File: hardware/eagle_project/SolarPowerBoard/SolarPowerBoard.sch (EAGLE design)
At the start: 77 parts, among them IC1 BQ29700DSET, IC3 TPS63031DSKT, J2 105017-0001, J5 XG8S-0331, K1 G6E-134P-US_DC5, Q3 FDN302P, U4 MCP73831T-2ACI/OT

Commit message: First check. Few things to modify:
- rearrange kelvin connections on sensing resistor (and routing around the fuel gauge)
- add LED on CBUS1 and CBUS2 of the FTDI chip (see powerDevPack project), or remove the CBUS1 and CBUS2 connections
- edit the JST connector footprint and increase holes size (see J5 footprint as reference)
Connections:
- net N$31 renamed USBDR_N
- net N$32 renamed USBDR_P
- net GND: no longer CHG2.EP, DCH2.EP
- net N$14: now also CHG2.EP, DCH2.EP
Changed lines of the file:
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@@
 <part name="GND32" library="supply1" library_urn="urn:adsk.eagle:library:371" deviceset="GND" device=""/>
 <part name="GND36" library="supply1" library_urn="urn:adsk.eagle:library:371" deviceset="GND" device=""/>
-<part name="GND23" library="supply1" library_urn="urn:adsk.eagle:library:371" deviceset="GND" device=""/>
-<part name="GND26" library="supply1" library_urn="urn:adsk.eagle:library:371" deviceset="GND" device=""/>
 <part name="J4" library="SolarComponents" deviceset="JST_2MM_MALE" device=""/>
 <part name="J3" library="SparkFun-Connectors" deviceset="CONN_01" device=""/>
@@
 <attribute name="VALUE" x="33.02" y="-30.48" size="1.778" layer="96" rot="R90"/>
 </instance>
-<instance part="GND23" gate="1" x="414.02" y="-20.32">
-<attribute name="VALUE" x="411.48" y="-22.86" size="1.778" layer="96"/>
-</instance>
-<instance part="GND26" gate="1" x="487.68" y="-20.32">
-<attribute name="VALUE" x="485.14" y="-22.86" size="1.778" layer="96"/>
-</instance>
 <instance part="J4" gate="G$1" x="479.806" y="46.99" rot="R90">
 <attribute name="NAME" x="473.964" y="44.45" size="1.778" layer="95" rot="R90"/>
@@
 <wire x1="17.78" y1="-27.94" x2="27.94" y2="-27.94" width="0.1524" layer="91"/>
 <pinref part="GND36" gate="1" pin="GND"/>
-</segment>
-<segment>
-<pinref part="CHG2" gate="G$1" pin="EP"/>
-<wire x1="414.02" y1="-12.7" x2="414.02" y2="-17.78" width="0.1524" layer="91"/>
-<pinref part="GND23" gate="1" pin="GND"/>
-</segment>
-<segment>
-<pinref part="DCH2" gate="G$1" pin="EP"/>
-<wire x1="487.68" y1="-12.7" x2="487.68" y2="-17.78" width="0.1524" layer="91"/>
-<pinref part="GND26" gate="1" pin="GND"/>
 </segment>
 <segment>
@@
 </segment>
 </net>
-<net name="N$31" class="0">
+<net name="USBDR_N" class="0">
 <segment>
 <pinref part="R23" gate="G$1" pin="1"/>
@@
 <wire x1="60.96" y1="152.4" x2="66.04" y2="152.4" width="0.1524" layer="91"/>
 <wire x1="66.04" y1="152.4" x2="66.04" y2="151.13" width="0.1524" layer="91"/>
-</segment>
-</net>
-<net name="N$32" class="0">
+<label x="60.96" y="152.4" size="1.778" layer="95"/>
+</segment>
+</net>
+<net name="USBDR_P" class="0">
 <segment>
 <pinref part="FT230XQ-R" gate="G$1" pin="USBDP"/>
@@
 <wire x1="66.04" y1="148.59" x2="66.04" y2="147.32" width="0.1524" layer="91"/>
 <wire x1="66.04" y1="147.32" x2="60.96" y2="147.32" width="0.1524" layer="91"/>
+<label x="58.42" y="144.78" size="1.778" layer="95"/>
 </segment>
 </net>
@@
 <wire x1="457.2" y1="10.16" x2="454.66" y2="10.16" width="0.1524" layer="91"/>
 <junction x="454.66" y="10.16"/>
-</segment>
-</net>
+<pinref part="CHG2" gate="G$1" pin="EP"/>
+<wire x1="414.02" y1="-12.7" x2="447.04" y2="-12.7" width="0.1524" layer="91"/>
+<wire x1="447.04" y1="-12.7" x2="447.04" y2="-5.08" width="0.1524" layer="91"/>
+<junction x="447.04" y="-5.08"/>
+<pinref part="DCH2" gate="G$1" pin="EP"/>
+<wire x1="487.68" y1="-12.7" x2="454.66" y2="-12.7" width="0.1524" layer="91"/>
+<wire x1="454.66" y1="-12.7" x2="454.66" y2="-5.08" width="0.1524" layer="91"/>
+<junction x="454.66" y="-5.08"/>
+</segment>
+</net>

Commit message: Fixed library link. Several small problems fixed.
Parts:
- added R27, R28: 470, SparkFun-Resistors:0.3OHM-0805-1/8W-1%
- added RX: ORANGE, SparkFun-LED:LED0603
- added TX: YELLOW, SparkFun-LED:LED0603
- AND: value 74AHC1G08DCK -> 74XX-LITTLE-DE_74AHC1G08DCK; device 74xx-little-de:74AHC1G08DCK -> SolarPowerBoard:74XX-LITTLE-DE_74AHC1G08DCK
- C1, C7, CMPP: device SparkFun-Capacitors:0.1UF-0603-100V-10% -> SolarPowerBoard:SPARKFUN-CAPACITORS_0.1UF-0603-100V-10%
- C1-1, C1-2: device SparkFun-Capacitors:4.7UF0603 -> SolarPowerBoard:SPARKFUN-CAPACITORS_4.7UF0603
- C10, COUT1, COUT2: device resistor:C-EUC0805 -> SolarPowerBoard:RESISTOR_C-EUC0805
- C11, C12: device SparkFun-Capacitors:CAP0603-CAP -> SolarPowerBoard:SPARKFUN-CAPACITORS_CAP0603-CAP
- C14: value 10uF -> 10nF; device SparkFun-Capacitors:10UF-0805-10V-10% -> SolarPowerBoard:SPARKFUN-CAPACITORS_10UF-0805-10V-10%:1
- C15, C16: value 10uF -> 47pF; device SparkFun-Capacitors:10UF-0805-10V-10% -> SolarPowerBoard:SPARKFUN-CAPACITORS_10UF-0805-10V-10%:1
- C2, C4: device SparkFun-Capacitors:10UF-0805-10V-10% -> SolarPowerBoard:SPARKFUN-CAPACITORS_10UF-0805-10V-10%
- C24, C26, C8, C9: value 10uF -> 100nF; device SparkFun-Capacitors:10UF-0805-10V-10% -> SolarPowerBoard:SPARKFUN-CAPACITORS_10UF-0805-10V-10%:1
- C25: value 10uF -> 4.7uF; device SparkFun-Capacitors:10UF-0805-10V-10% -> SolarPowerBoard:SPARKFUN-CAPACITORS_10UF-0805-10V-10%:1
- C3: value 10UF -> 10uF; device SparkFun-Capacitors:10UF-0805-10V-10% -> SolarPowerBoard:SPARKFUN-CAPACITORS_10UF-0805-10V-10%
- C5: device SparkFun-Capacitors:0.1UF-0603-25V-5% -> SolarPowerBoard:SPARKFUN-CAPACITORS_0.1UF-0603-25V-5%
- C6: device SparkFun-Capacitors:470PF-0603-50V-5% -> SolarPowerBoard:SPARKFUN-CAPACITORS_470PF-0603-50V-5%
- CF: device SparkFun-Capacitors:1.0UF-0805-25V-(+80/-20%) -> SolarPowerBoard:SPARKFUN-CAPACITORS_1.0UF-0805-25V-(+80/-20%)
- CHG2, DCH2: value CSD16406Q3 -> SOLARCOMPONENTS_CSD16406Q3; device SolarComponents:CSD16406Q3 -> SolarPowerBoard:SOLARCOMPONENTS_CSD16406Q3
- D5: device SparkFun-LED:LED0603 -> SolarPowerBoard:SPARKFUN-LED_LED0603
- FT230XQ-R: device FT230XQ:FT230XQ_2 -> SolarPowerBoard:FT230XQ_FT230XQ_2
- IC1: value BQ29700DSET -> BQ29700DSET_BQ29700DSET; device BQ29700DSET:BQ29700DSET -> SolarPowerBoard:BQ29700DSET_BQ29700DSET
- IC3: value TPS63031DSKT -> TPS63031DSKT_TPS63031DSKT; device TPS63031DSKT:TPS63031DSKT -> SolarPowerBoard:TPS63031DSKT_TPS63031DSKT
- J2: value 105017-0001 -> 105017-0001_105017-0001; device 105017-0001:105017-0001 -> SolarPowerBoard:105017-0001_105017-0001
- J3: device SparkFun-Connectors:CONN_01 -> SolarPowerBoard:SPARKFUN-CONNECTORS_CONN_01
- J4, J6: device SolarComponents:JST_2MM_MALE -> SolarPowerBoard:SOLARCOMPONENTS_JST_2MM_MALE
- J5: value XG8S-0331 -> XG8S-0331_XG8S-0331; device XG8S-0331:XG8S-0331 -> SolarPowerBoard:XG8S-0331_XG8S-0331
- JP1: value JUMPER-SMT_3_1-NC_TRACE_NO-SILK -> SPARKFUN-JUMPERS_JUMPER-SMT_3_1-NC_TRACE_NO-SILK; device SparkFun-Jumpers:JUMPER-SMT_3_1-NC_TRACE_NO-SILK -> SolarPowerBoard:SPARKFUN-JUMPERS_JUMPER-SMT_3_1-NC_TRACE_NO-SILK
- K1: value G6E-134P-US_DC5 -> G6E-134P-US_DC5_G6E-134P-US_DC5; device G6E-134P-US_DC5:G6E-134P-US_DC5 -> SolarPowerBoard:G6E-134P-US_DC5_G6E-134P-US_DC5
- L1: value SRR1280-270M -> SOLARPOWERBOARD_SRR1280-270M; device SolarPowerBoard:SRR1280-270M -> SolarPowerBoard:SOLARPOWERBOARD_SRR1280-270M
- L2: value SRN3010-470M -> SRN3010-470M_SRN3010-470M; device SRN3010-470M:SRN3010-470M -> SolarPowerBoard:SRN3010-470M_SRN3010-470M
- L3: device davide:FERRITE_BREAD -> SolarPowerBoard:DAVIDE_FERRITE_BREAD
- Q3: value FDN302P -> DAVIDE_FDN302P; device davide:FDN302P -> SolarPowerBoard:DAVIDE_FDN302P
- R1, R2, R3, R8, RF1, RF2, RGS1, RGS2, RTEMP: device resistor:R-US_R0805 -> SolarPowerBoard:RESISTOR_R-US_R0805
- R10: value 330 -> (none); device SparkFun-Resistors:RESISTOR0805 -> SolarPowerBoard:SPARKFUN-RESISTORS_RESISTOR0805:1
- R14, R25: value 0.3 -> 100k; device SparkFun-Resistors:0.3OHM-0805-1/8W-1% -> SolarPowerBoard:SPARKFUN-RESISTORS_0.3OHM-0805-1/8W-1%
- R15: device SparkFun-Resistors:0.3OHM-0805-1/8W-1% -> SolarPowerBoard:SPARKFUN-RESISTORS_0.3OHM-0805-1/8W-1%
- R23, R29: value 0.3 -> 27; device SparkFun-Resistors:0.3OHM-0805-1/8W-1% -> SolarPowerBoard:SPARKFUN-RESISTORS_0.3OHM-0805-1/8W-1%
- R24: value 0.3 -> DNM; device SparkFun-Resistors:0.3OHM-0805-1/8W-1% -> SolarPowerBoard:SPARKFUN-RESISTORS_0.3OHM-0805-1/8W-1%
- R26: value 0.3 -> 1k; device SparkFun-Resistors:0.3OHM-0805-1/8W-1% -> SolarPowerBoard:SPARKFUN-RESISTORS_0.3OHM-0805-1/8W-1%
- R9: value 2.2k -> (none); device SparkFun-Resistors:RESISTOR0805 -> SolarPowerBoard:SPARKFUN-RESISTORS_RESISTOR0805:1
- RB2: value CC2650LAUNCHPAD -> POWERSOL_CC2650LAUNCHPAD; device powersol:CC2650LAUNCHPAD -> SolarPowerBoard:POWERSOL_CC2650LAUNCHPAD
- RCG3: value 1mOhm -> (none); device SparkFun-Resistors:RESISTOR0805 -> SolarPowerBoard:SPARKFUN-RESISTORS_RESISTOR0805:1
- RGPIO1, RGPIO2, RGPIO3, RGPIO4: device SparkFun-Resistors:RESISTOR0603 -> SolarPowerBoard:SPARKFUN-RESISTORS_RESISTOR0603:1
- RLED1, RPROG1: device SparkFun-Passives:RESISTOR0603-RES -> SolarPowerBoard:SPARKFUN-PASSIVES_RESISTOR0603-RES
- RS1: value RL1220T-R010-J -> RL1220T-R010-J_RL1220T-R010-J; device RL1220T-R010-J:RL1220T-R010-J -> SolarPowerBoard:RL1220T-R010-J_RL1220T-R010-J
- RX_TX: device SparkFun-Connectors:CONN_04 -> SolarPowerBoard:SPARKFUN-CONNECTORS_CONN_04
- SCL, SDA: value JUMPER-SMT_3_0_SILK -> POWERSOL_JUMPER-SMT_3_0_SILK; device powersol:JUMPER-SMT_3_0_SILK -> SolarPowerBoard:POWERSOL_JUMPER-SMT_3_0_SILK
- SCL_SDA: device SparkFun-Connectors:CONN_02 -> SolarPowerBoard:SPARKFUN-CONNECTORS_CONN_02
- U$1: value SVP1040 -> SOLARCOMPONENTS_SVP1040; device SolarComponents:SVP1040 -> SolarPowerBoard:SOLARCOMPONENTS_SVP1040
- U$2: value PCA10040NORDIC -> POWERSOL_PCA10040NORDIC; device powersol:PCA10040NORDIC -> SolarPowerBoard:POWERSOL_PCA10040NORDIC
- U$3: value MAX17260 -> SOLARCOMPONENTS_MAX17260; device SolarComponents:MAX17260 -> SolarPowerBoard:SOLARCOMPONENTS_MAX17260
- U4: value MCP73831T-2ACI/OT -> MCP73831T-2ACI_OT_MCP73831T-2ACI/OT; device MCP73831T-2ACI_OT:MCP73831T-2ACI/OT -> SolarPowerBoard:MCP73831T-2ACI_OT_MCP73831T-2ACI/OT
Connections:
- new net N$31: FT230XQ-R.CBUS0, R28.1
- new net N$32: R28.2, RX.C
- new net N$42: R27.2, TX.C
- new net N$43: FT230XQ-R.CBUS2, R27.1
- net VCCIO_FTDI: now also RX.A, TX.A; no longer FT230XQ-R.CBUS1, FT230XQ-R.CBUS2

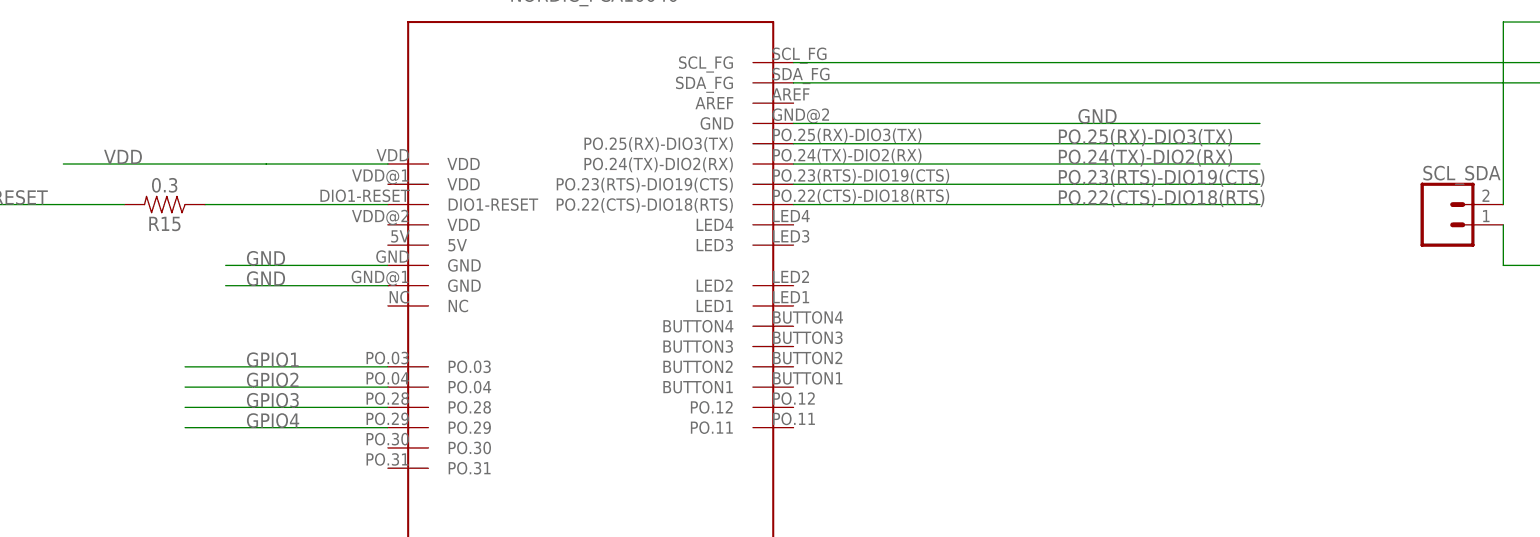
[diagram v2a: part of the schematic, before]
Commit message: Added Nordic TX pin pull up resistor
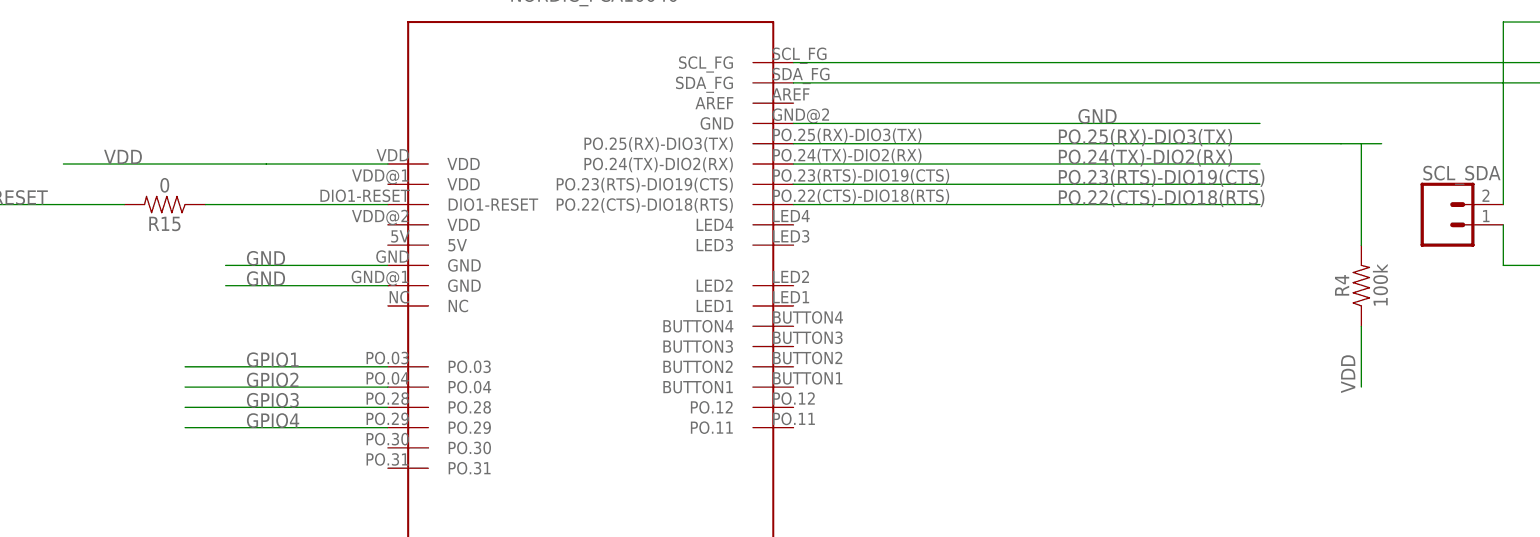
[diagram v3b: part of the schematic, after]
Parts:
- added R4: 100k, SolarPowerBoard:SPARKFUN-RESISTORS_0.3OHM-0805-1/8W-1%
- R15: value 0.3 -> 0
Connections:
- net PO.25(RX)-DIO3(TX): now also R4.2
- net VDD: now also R4.1
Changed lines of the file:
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@@
 <attribute name="OC_NEWARK" value="82Y0957"/>
 </part>
-<part name="R15" library="SolarPowerBoard" deviceset="SPARKFUN-RESISTORS_0.3OHM" device="-0805-1/8W-1%" value="0.3">
+<part name="R15" library="SolarPowerBoard" deviceset="SPARKFUN-RESISTORS_0.3OHM" device="-0805-1/8W-1%" value="0">
 <attribute name="MF" value=""/>
 <attribute name="MPN" value="RLP73N2AR30JTD"/>
@@
 <part name="R27" library="SparkFun-Resistors" library_urn="urn:adsk.eagle:library:532" deviceset="0.3OHM" device="-0805-1/8W-1%" package3d_urn="urn:adsk.eagle:package:39651/1" value="470"/>
 <part name="R28" library="SparkFun-Resistors" library_urn="urn:adsk.eagle:library:532" deviceset="0.3OHM" device="-0805-1/8W-1%" package3d_urn="urn:adsk.eagle:package:39651/1" value="470"/>
+<part name="R4" library="SolarPowerBoard" deviceset="SPARKFUN-RESISTORS_0.3OHM" device="-0805-1/8W-1%" value="100k">
+<attribute name="MF" value=""/>
+<attribute name="MPN" value="RLP73N2AR30JTD"/>
+<attribute name="OC_NEWARK" value="43AC3996"/>
+</part>
 </parts>
 <sheets>
@@
 <attribute name="NAME" x="145.034" y="147.32" size="1.778" layer="95" font="vector" rot="R90" align="bottom-center"/>
 <attribute name="VALUE" x="148.082" y="147.32" size="1.778" layer="96" font="vector" rot="R90" align="top-center"/>
+</instance>
+<instance part="R4" gate="G$1" x="-391.16" y="17.78" rot="R90">
+<attribute name="OC_NEWARK" x="-391.16" y="17.78" size="1.778" layer="96" rot="R270" display="off"/>
+<attribute name="MF" x="-391.16" y="17.78" size="1.778" layer="96" rot="R270" display="off"/>
+<attribute name="MPN" x="-391.16" y="17.78" size="1.778" layer="96" rot="R270" display="off"/>
+<attribute name="NAME" x="-392.684" y="17.78" size="1.778" layer="95" font="vector" rot="R90" align="bottom-center"/>
+<attribute name="VALUE" x="-389.636" y="17.78" size="1.778" layer="96" font="vector" rot="R90" align="top-center"/>
 </instance>
 </instances>
@@
 <junction x="-48.26" y="-35.56"/>
 </segment>
+<segment>
+<pinref part="R4" gate="G$1" pin="1"/>
+<wire x1="-391.16" y1="12.7" x2="-391.16" y2="5.08" width="0.1524" layer="91"/>
+<label x="-391.922" y="4.318" size="1.778" layer="95" rot="R90"/>
+</segment>
 </net>
 <net name="PO.25(RX)-DIO3(TX)" class="0">
 <segment>
-<wire x1="-462.28" y1="35.56" x2="-403.86" y2="35.56" width="0.1524" layer="91"/>
+<wire x1="-462.28" y1="35.56" x2="-393.7" y2="35.56" width="0.1524" layer="91"/>
 <label x="-429.26" y="35.56" size="1.778" layer="95"/>
 <pinref part="U$2" gate="G$1" pin="PO.25(RX)-DIO3(TX)"/>
-</segment>
-<segment>
+<wire x1="-391.16" y1="35.56" x2="-388.62" y2="35.56" width="0.1524" layer="91"/>
+<wire x1="-393.7" y1="35.56" x2="-391.16" y2="35.56" width="0.1524" layer="91"/>
+<wire x1="-391.16" y1="35.56" x2="-391.16" y2="22.86" width="0.1524" layer="91"/>
+<pinref part="R4" gate="G$1" pin="2"/>
+</segment>
+<segment>

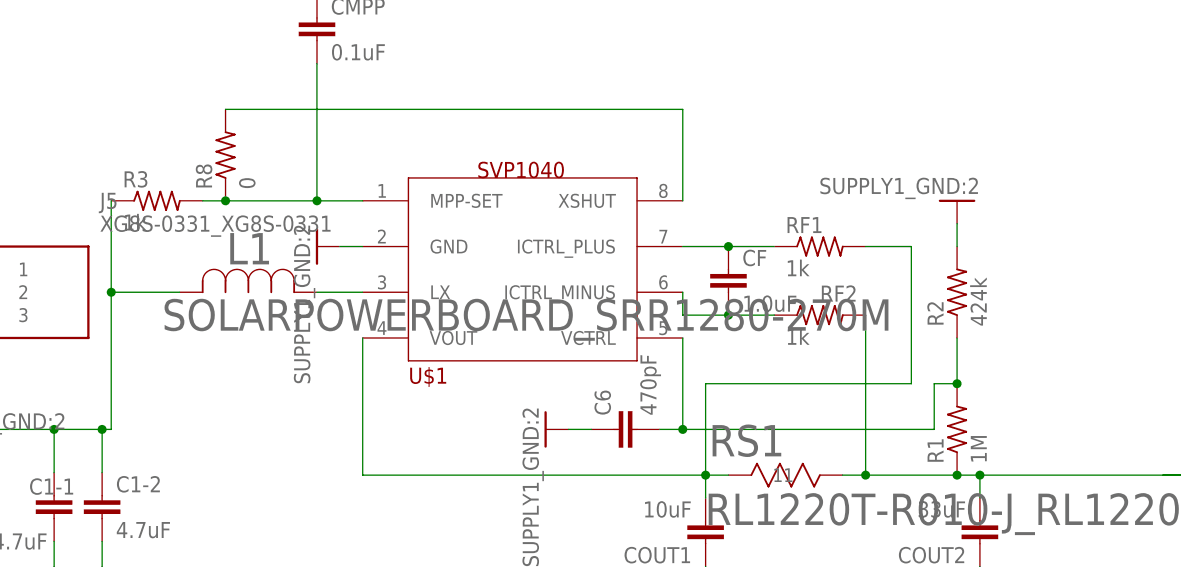
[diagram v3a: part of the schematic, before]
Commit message: Changed inductor footprint
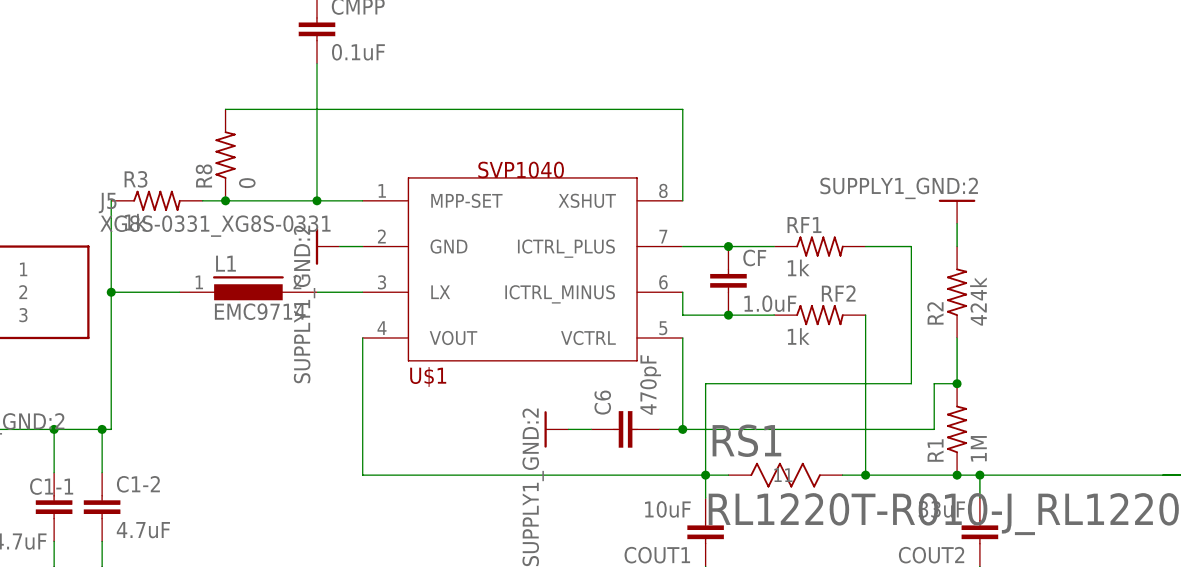
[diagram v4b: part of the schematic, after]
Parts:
- L1: value SOLARPOWERBOARD_SRR1280-270M -> EMC9714; device SolarPowerBoard:SOLARPOWERBOARD_SRR1280-270M -> inductors:EMC9714
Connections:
- net N$1: now also L1.1; no longer L1.2
- net N$18: now also L1.2; no longer L1.1
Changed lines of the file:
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@@
 <part name="GND1" library="SolarPowerBoard" deviceset="SUPPLY1_GND*?:2" device=""/>
 <part name="RS1" library="SolarPowerBoard" deviceset="RL1220T-R010-J_RL1220T-R010-J" device=""/>
-<part name="L1" library="SolarPowerBoard" deviceset="SOLARPOWERBOARD_SRR1280-270M" device=""/>
 <part name="J5" library="SolarPowerBoard" deviceset="XG8S-0331_XG8S-0331" device=""/>
 <part name="K1" library="SolarPowerBoard" deviceset="G6E-134P-US_DC5_G6E-134P-US_DC5" device=""/>
@@
 <attribute name="OC_NEWARK" value="43AC3996"/>
 </part>
+<part name="L1" library="inductors" library_urn="urn:adsk.eagle:library:243" deviceset="EMC9714" device="" package3d_urn="urn:adsk.eagle:package:15060/1"/>
 </parts>
 <sheets>
@@
 </instance>
 <instance part="GND3" gate="1" x="35.56" y="111.76" rot="R180"/>
-<instance part="GND4" gate="1" x="35.56" y="78.74" rot="R270">
-<attribute name="VALUE" x="33.02" y="81.28" size="1.778" layer="96" rot="R270"/>
-</instance>
+<instance part="GND4" gate="1" x="35.56" y="78.74" rot="R270"/>
 <instance part="GND5" gate="1" x="106.68" y="83.82" rot="R180">
 <attribute name="VALUE" x="109.22" y="86.36" size="1.778" layer="96" rot="R180"/>
@@
 <attribute name="NAME" x="79.0956" y="55.4228" size="3.4798" layer="95" ratio="10" rot="SR0"/>
 </instance>
-<instance part="L1" gate="A" x="20.32" y="73.66">
-<attribute name="NAME" x="25.5016" y="76.7588" size="3.4798" layer="95" ratio="10" rot="SR0"/>
-</instance>
 <instance part="J5" gate="G$1" x="-5.08" y="76.2">
 <attribute name="NAME" x="11.43" y="83.82" size="1.778" layer="95" align="center-left"/>
@@
 <attribute name="NAME" x="-392.684" y="17.78" size="1.778" layer="95" font="vector" rot="R90" align="bottom-center"/>
 <attribute name="VALUE" x="-389.636" y="17.78" size="1.778" layer="96" font="vector" rot="R90" align="top-center"/>
+</instance>
+<instance part="L1" gate="1" x="27.94" y="73.66">
+<attribute name="NAME" x="24.13" y="75.946" size="1.778" layer="95"/>
+<attribute name="VALUE" x="24.003" y="70.612" size="1.778" layer="96"/>
 </instance>
 </instances>
@@
 <junction x="6.35" y="58.42"/>
 <pinref part="R3" gate="G$1" pin="1"/>
-<pinref part="L1" gate="A" pin="2"/>
 <wire x1="12.7" y1="73.66" x2="20.32" y2="73.66" width="0.1524" layer="91"/>
 <junction x="12.7" y="73.66"/>
@@
 <wire x1="-5.08" y1="71.12" x2="-5.08" y2="58.42" width="0.1524" layer="91"/>
 <wire x1="-5.08" y1="58.42" x2="6.35" y2="58.42" width="0.1524" layer="91"/>
+<pinref part="L1" gate="1" pin="1"/>
 </segment>
 </net>
@@
 <net name="N$18" class="0">
 <segment>
-<pinref part="L1" gate="A" pin="1"/>
 <pinref part="U$1" gate="G$1" pin="LX"/>
 <wire x1="35.56" y1="73.66" x2="40.64" y2="73.66" width="0.1524" layer="91"/>
+<pinref part="L1" gate="1" pin="2"/>
 </segment>
 </net>
@@
 packages will not be understood (or retained) with this version.
 </note>
+<note version="8.4" severity="warning">
+Since Version 8.4, EAGLE supports properties for SPICE simulation.
+Probes in schematics and SPICE mapping objects found in parts and library devices
+will not be understood with this version. Update EAGLE to the latest version
+for full support of SPICE simulation.
+</note>
 </compatibility>
